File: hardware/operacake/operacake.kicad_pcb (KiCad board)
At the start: 4 copper layers, 120 x 75 mm, 129 parts, among them J1 CONN_02X20, J2 CONN_02X20, P1 ADDRESS, P20 GPIO, P22 I2S, P28 SD, P9 BASEBAND, U1 MASWSS0129, U10 74LVC1G58, U11 74LVC1G58, U12 74LVC1G58, U13 74LVC1G58, U14 74AHC1G02, U15 74AHC1G02, U16 74LVC1G19, U2 SKY13322, U3 SKY13322, U4 PCA9557, U5 TC7MBL3245CFT, U6 74LVC1G58, U7 74LVC1G58, U8 74AHC1G08, U9 74AHC1G08

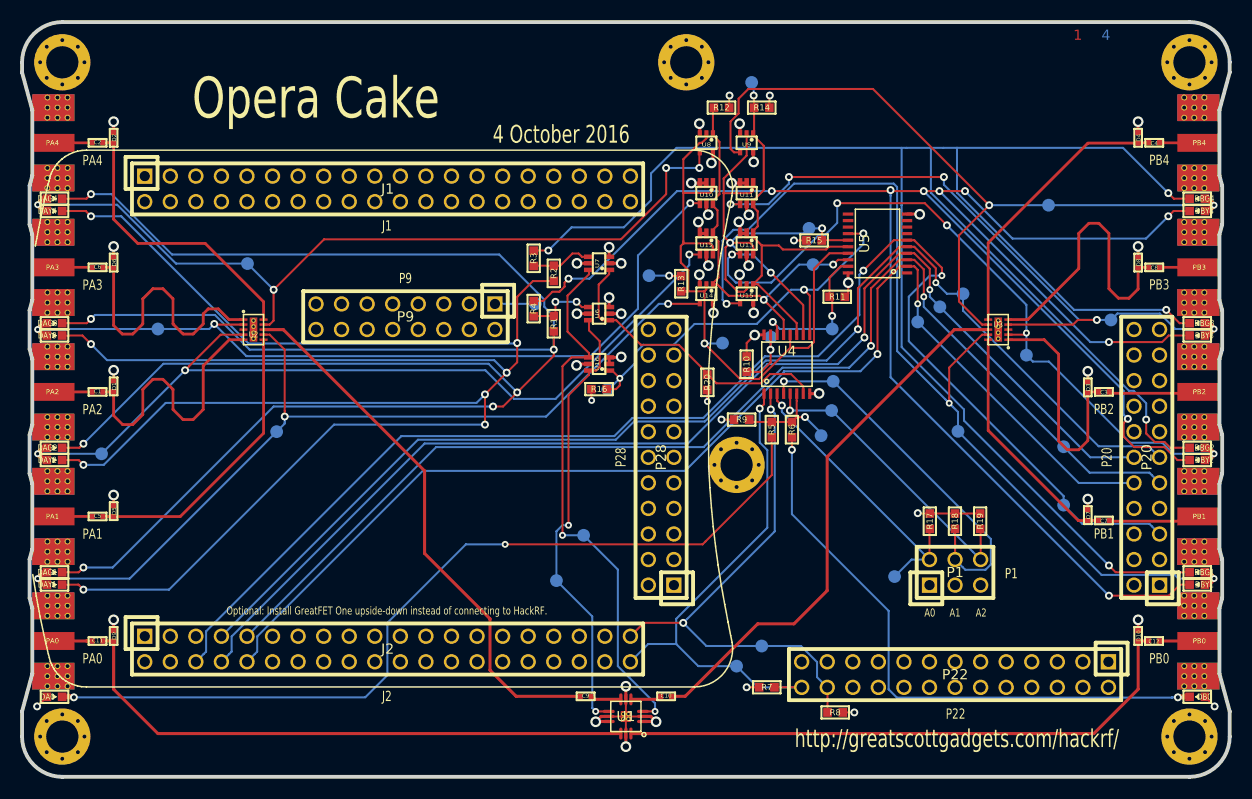
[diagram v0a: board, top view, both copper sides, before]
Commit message: Added decoupling capacitors.
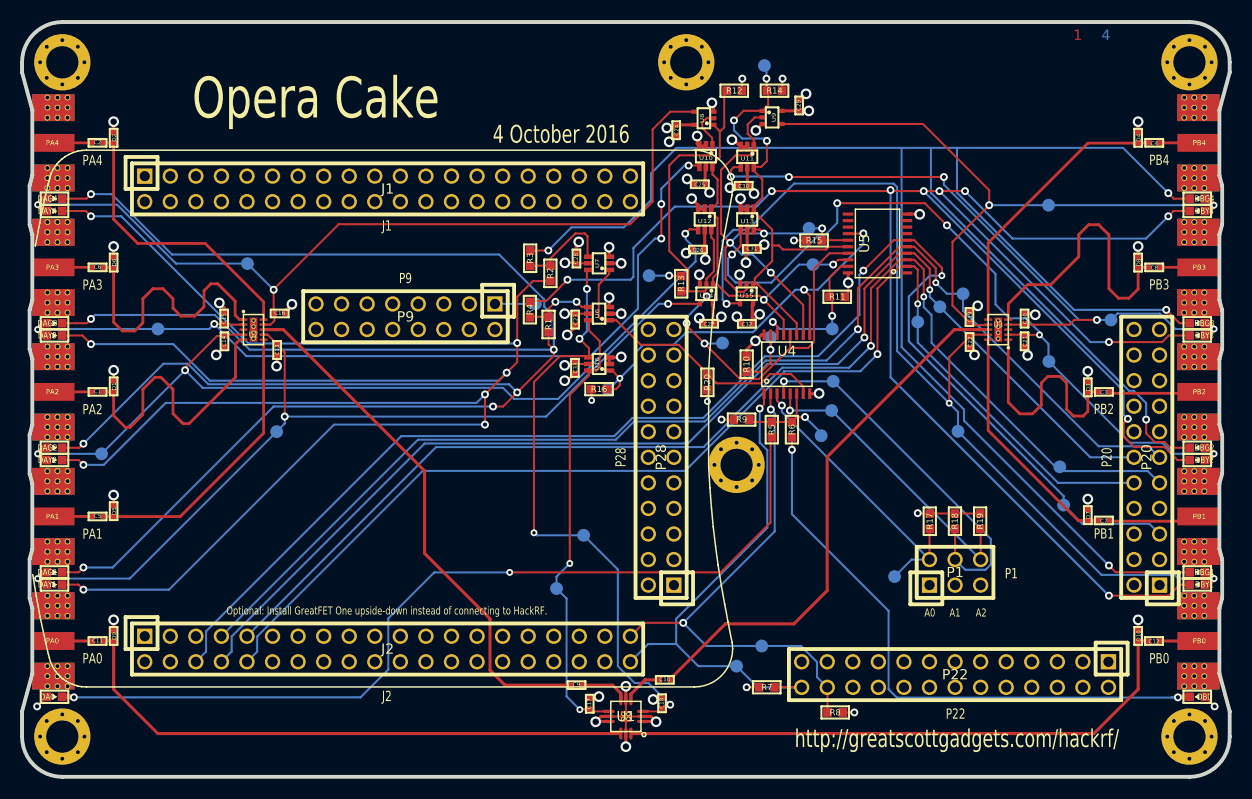
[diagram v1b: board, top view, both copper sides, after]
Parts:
- added C13: 33pF, gsg-modules:0402, F.Cu at (85.3, 132.6)
- added C14: 33pF, gsg-modules:0402, F.Cu at (80.1, 131.7)
- added C15: 33pF, gsg-modules:0402, F.Cu at (80.1, 129.5)
- added C16: 33pF, gsg-modules:0402, F.Cu at (85.6, 129.0)
- added C17: 33pF, gsg-modules:0402, F.Cu at (116.4, 167.7)
- added C18: 33pF, gsg-modules:0402, F.Cu at (123.6, 167.7)
- added C19: 33pF, gsg-modules:0402, F.Cu at (154.1, 129.3)
- added C20: 33pF, gsg-modules:0402, F.Cu at (159.6, 129.5)
- added C21: 33pF, gsg-modules:0402, F.Cu at (159.6, 131.7)
- added C22: 33pF, gsg-modules:0402, F.Cu at (154.2, 131.8)
- added C23: 100nF, gsg-modules:0402, F.Cu at (115.0, 129.6)
- added C24: 100nF, gsg-modules:0402, F.Cu at (125.0, 110.7)
- added C25: 100nF, gsg-modules:0402, F.Cu at (127.3, 116.1)
- added C26: 100nF, gsg-modules:0402, F.Cu at (127.2, 122.6)
- added C27: 100nF, gsg-modules:0402, F.Cu at (128.3, 130.0)
- added C28: 100nF, gsg-modules:0402, F.Cu at (115.1, 123.5)
- added C29: 100nF, gsg-modules:0402, F.Cu at (137.2, 108.3)
- added C30: 100nF, gsg-modules:0402, F.Cu at (131.7, 116.3)
- added C31: 100nF, gsg-modules:0402, F.Cu at (132.5, 122.5)
- added C32: 100nF, gsg-modules:0402, F.Cu at (132.0, 130.0)
- added C33: 100nF, gsg-modules:0402, F.Cu at (114.9, 134.4)
- C1, C10, C11, C12, C2, C3, C4, C5, C6, C7, C8, C9: value C -> 100nF
- moved U10 3.68 mm to (128.0, 113.3)
- moved U11 3.61 mm to (132.1, 113.4)
- moved U9 3.57 mm to (134.5, 109.5), turned to 270 degrees
- moved U8 2.45 mm to (127.8, 109.6), turned to 90 degrees
- moved U12 2.40 mm to (127.8, 119.6)
- moved U13 2.38 mm to (132.1, 119.6)
- moved TP23 2.32 mm to (162.0, 133.7)
- moved R12 2.10 mm to (130.8, 106.8)
- moved R14 2.10 mm to (134.8, 106.8)
- moved TP13 2.10 mm to (133.8, 104.3)
- moved TP2 2.04 mm to (163.1, 144.2)
- moved C10 1.64 mm to (123.9, 165.4)
- moved C9 1.44 mm to (115.1, 165.9)
- moved TP17 0.79 mm to (113.1, 156.3)
- moved R1 0.52 mm to (112.3, 130.0)
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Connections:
- J1 pad 10: (no net) -> Net-(J1-Pad10)
- J1 pad 11: (no net) -> Net-(J1-Pad11)
- J1 pad 12: (no net) -> Net-(J1-Pad12)
- J1 pad 13: (no net) -> Net-(J1-Pad13)
- J1 pad 14: (no net) -> Net-(J1-Pad14)
- J1 pad 15: (no net) -> Net-(J1-Pad15)
- J1 pad 16: (no net) -> Net-(J1-Pad16)
- J1 pad 17: (no net) -> Net-(J1-Pad17)
- J1 pad 18: (no net) -> Net-(J1-Pad18)
- J1 pad 19: (no net) -> Net-(J1-Pad19)
- J1 pad 20: (no net) -> Net-(J1-Pad20)
- J1 pad 21: (no net) -> Net-(J1-Pad21)
- J1 pad 22: (no net) -> Net-(J1-Pad22)
- J1 pad 23: (no net) -> Net-(J1-Pad23)
- J1 pad 24: (no net) -> Net-(J1-Pad24)
- J1 pad 25: (no net) -> Net-(J1-Pad25)
- J1 pad 26: (no net) -> Net-(J1-Pad26)
- J1 pad 27: (no net) -> Net-(J1-Pad27)
- J1 pad 28: (no net) -> Net-(J1-Pad28)
- J1 pad 29: (no net) -> Net-(J1-Pad29)
- J1 pad 3: (no net) -> Net-(J1-Pad3)
- J1 pad 30: (no net) -> Net-(J1-Pad30)
- J1 pad 31: (no net) -> Net-(J1-Pad31)
- J1 pad 32: (no net) -> Net-(J1-Pad32)
- J1 pad 33: (no net) -> Net-(J1-Pad33)
- J1 pad 34: (no net) -> Net-(J1-Pad34)
- J1 pad 35: (no net) -> Net-(J1-Pad35)
- J1 pad 36: (no net) -> Net-(J1-Pad36)
- J1 pad 37: (no net) -> Net-(J1-Pad37)
- J1 pad 38: (no net) -> Net-(J1-Pad38)
- J1 pad 39: (no net) -> Net-(J1-Pad39)
- J1 pad 4: (no net) -> Net-(J1-Pad4)
- J1 pad 40: (no net) -> Net-(J1-Pad40)
- J1 pad 5: (no net) -> Net-(J1-Pad5)
- J1 pad 6: (no net) -> Net-(J1-Pad6)
- J1 pad 7: (no net) -> Net-(J1-Pad7)
- J1 pad 8: (no net) -> Net-(J1-Pad8)
- J1 pad 9: (no net) -> Net-(J1-Pad9)
- J2 pad 11: (no net) -> Net-(J2-Pad11)
- J2 pad 12: (no net) -> Net-(J2-Pad12)
- J2 pad 13: (no net) -> Net-(J2-Pad13)
- J2 pad 14: (no net) -> Net-(J2-Pad14)
- J2 pad 15: (no net) -> Net-(J2-Pad15)
- J2 pad 16: (no net) -> Net-(J2-Pad16)
- J2 pad 17: (no net) -> Net-(J2-Pad17)
- J2 pad 18: (no net) -> Net-(J2-Pad18)
- J2 pad 19: (no net) -> Net-(J2-Pad19)
- J2 pad 2: (no net) -> Net-(J2-Pad2)
- J2 pad 20: (no net) -> Net-(J2-Pad20)
- J2 pad 21: (no net) -> Net-(J2-Pad21)
- J2 pad 22: (no net) -> Net-(J2-Pad22)
- J2 pad 23: (no net) -> Net-(J2-Pad23)
- J2 pad 24: (no net) -> Net-(J2-Pad24)
- J2 pad 25: (no net) -> Net-(J2-Pad25)
- J2 pad 26: (no net) -> Net-(J2-Pad26)
- J2 pad 27: (no net) -> Net-(J2-Pad27)
- J2 pad 28: (no net) -> Net-(J2-Pad28)
- J2 pad 29: (no net) -> Net-(J2-Pad29)
- J2 pad 3: (no net) -> Net-(J2-Pad3)
- J2 pad 30: (no net) -> Net-(J2-Pad30)
- J2 pad 31: (no net) -> Net-(J2-Pad31)
- J2 pad 32: (no net) -> Net-(J2-Pad32)
- J2 pad 33: (no net) -> Net-(J2-Pad33)
- J2 pad 34: (no net) -> Net-(J2-Pad34)
- J2 pad 35: (no net) -> Net-(J2-Pad35)
- J2 pad 36: (no net) -> Net-(J2-Pad36)
- J2 pad 37: (no net) -> Net-(J2-Pad37)
- J2 pad 38: (no net) -> Net-(J2-Pad38)
- J2 pad 4: (no net) -> Net-(J2-Pad4)
- J2 pad 5: (no net) -> Net-(J2-Pad5)
- P20 pad 1: (no net) -> Net-(P20-Pad1)
- P20 pad 14: (no net) -> Net-(P20-Pad14)
- P20 pad 16: (no net) -> Net-(P20-Pad16)
- P20 pad 17: (no net) -> Net-(P20-Pad17)
- P20 pad 18: (no net) -> Net-(P20-Pad18)
- P20 pad 2: (no net) -> Net-(P20-Pad2)
- P20 pad 20: (no net) -> Net-(P20-Pad20)
- P20 pad 21: (no net) -> Net-(P20-Pad21)
- P20 pad 22: (no net) -> Net-(P20-Pad22)
- P20 pad 4: (no net) -> Net-(P20-Pad4)
- P20 pad 6: (no net) -> Net-(P20-Pad6)
- P20 pad 7: (no net) -> Net-(P20-Pad7)
- P20 pad 8: (no net) -> Net-(P20-Pad8)
- P22 pad 1: (no net) -> Net-(P22-Pad1)
- P22 pad 12: (no net) -> Net-(P22-Pad12)
- P22 pad 13: (no net) -> Net-(P22-Pad13)
- P22 pad 14: (no net) -> Net-(P22-Pad14)
- P22 pad 15: (no net) -> Net-(P22-Pad15)
- P22 pad 16: (no net) -> Net-(P22-Pad16)
- P22 pad 17: (no net) -> Net-(P22-Pad17)
- P22 pad 19: (no net) -> Net-(P22-Pad19)
- P22 pad 2: (no net) -> Net-(P22-Pad2)
- P22 pad 20: (no net) -> Net-(P22-Pad20)
- P22 pad 21: (no net) -> Net-(P22-Pad21)
- P22 pad 22: (no net) -> Net-(P22-Pad22)
- P22 pad 23: (no net) -> Net-(P22-Pad23)
- P22 pad 25: (no net) -> Net-(P22-Pad25)
- P22 pad 3: (no net) -> Net-(P22-Pad3)
- P22 pad 5: (no net) -> Net-(P22-Pad5)
- P22 pad 6: (no net) -> Net-(P22-Pad6)
- P22 pad 7: (no net) -> Net-(P22-Pad7)
- P22 pad 8: (no net) -> Net-(P22-Pad8)
- P22 pad 9: (no net) -> Net-(P22-Pad9)
- P28 pad 10: (no net) -> Net-(P28-Pad10)
- P28 pad 11: (no net) -> Net-(P28-Pad11)
- P28 pad 13: (no net) -> Net-(P28-Pad13)
- P28 pad 14: (no net) -> Net-(P28-Pad14)
- P28 pad 15: (no net) -> Net-(P28-Pad15)
- P28 pad 16: (no net) -> Net-(P28-Pad16)
- P28 pad 17: (no net) -> Net-(P28-Pad17)
- P28 pad 18: (no net) -> Net-(P28-Pad18)
- P28 pad 19: (no net) -> Net-(P28-Pad19)
- P28 pad 20: (no net) -> Net-(P28-Pad20)
- P28 pad 21: (no net) -> Net-(P28-Pad21)
- P28 pad 22: (no net) -> Net-(P28-Pad22)
- P28 pad 3: (no net) -> Net-(P28-Pad3)
- P28 pad 4: (no net) -> Net-(P28-Pad4)
- P28 pad 5: (no net) -> Net-(P28-Pad5)
- P28 pad 6: (no net) -> Net-(P28-Pad6)
- P28 pad 7: (no net) -> Net-(P28-Pad7)
- P28 pad 8: (no net) -> Net-(P28-Pad8)
- P28 pad 9: (no net) -> Net-(P28-Pad9)
- P9 pad 10: (no net) -> Net-(P9-Pad10)
- P9 pad 11: (no net) -> Net-(P9-Pad11)
- P9 pad 12: (no net) -> Net-(P9-Pad12)
- P9 pad 13: (no net) -> Net-(P9-Pad13)
- P9 pad 4: (no net) -> Net-(P9-Pad4)
- P9 pad 5: (no net) -> Net-(P9-Pad5)
- P9 pad 6: (no net) -> Net-(P9-Pad6)
- P9 pad 7: (no net) -> Net-(P9-Pad7)
- U2 pad 3: (no net) -> Net-(U2-Pad3)
- U3 pad 3: (no net) -> Net-(U3-Pad3)
- U5 pad 1: (no net) -> Net-(U5-Pad1)
- U5 pad 11: (no net) -> Net-(U5-Pad11)
- U5 pad 12: (no net) -> Net-(U5-Pad12)
- U5 pad 13: (no net) -> Net-(U5-Pad13)
- U5 pad 7: (no net) -> Net-(U5-Pad7)
- U5 pad 8: (no net) -> Net-(U5-Pad8)
- U5 pad 9: (no net) -> Net-(U5-Pad9)
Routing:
- net GND: track 55.6 -> 85.6 mm, vias 29 -> 49
- net VCC: track 34.9 -> 53.0 mm
- net /U3V3: track 75.8 -> 65.4 mm
- net /U3CTRL1: track 38.1 -> 45.4 mm, vias 1 -> 3
- net /U1VC1: track 54.0 -> 60.1 mm, vias 2 -> 4
- net /U2CTRL0: track 62.2 -> 68.1 mm, vias 1 -> 3
- net /U2V2: track 82.1 -> 86.6 mm, vias 3 -> 5
- net Net-(R2-Pad2): track 6.15 -> 10.1 mm
- net /U2V1: track 86.6 -> 90.0 mm
- net /U3V2: track 73.5 -> 76.8 mm
- net /U2V4: track 84.1 -> 87.3 mm, vias 4 -> 2
- net /U2CTRL1: track 39.0 -> 41.9 mm
- net Net-(DA0-Pad1): track 86.5 -> 89.1 mm
- net Net-(C9-Pad1): track 3.09 -> 5.14 mm
- net /EXT_U2CTRL0: track 120.9 -> 122.6 mm
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
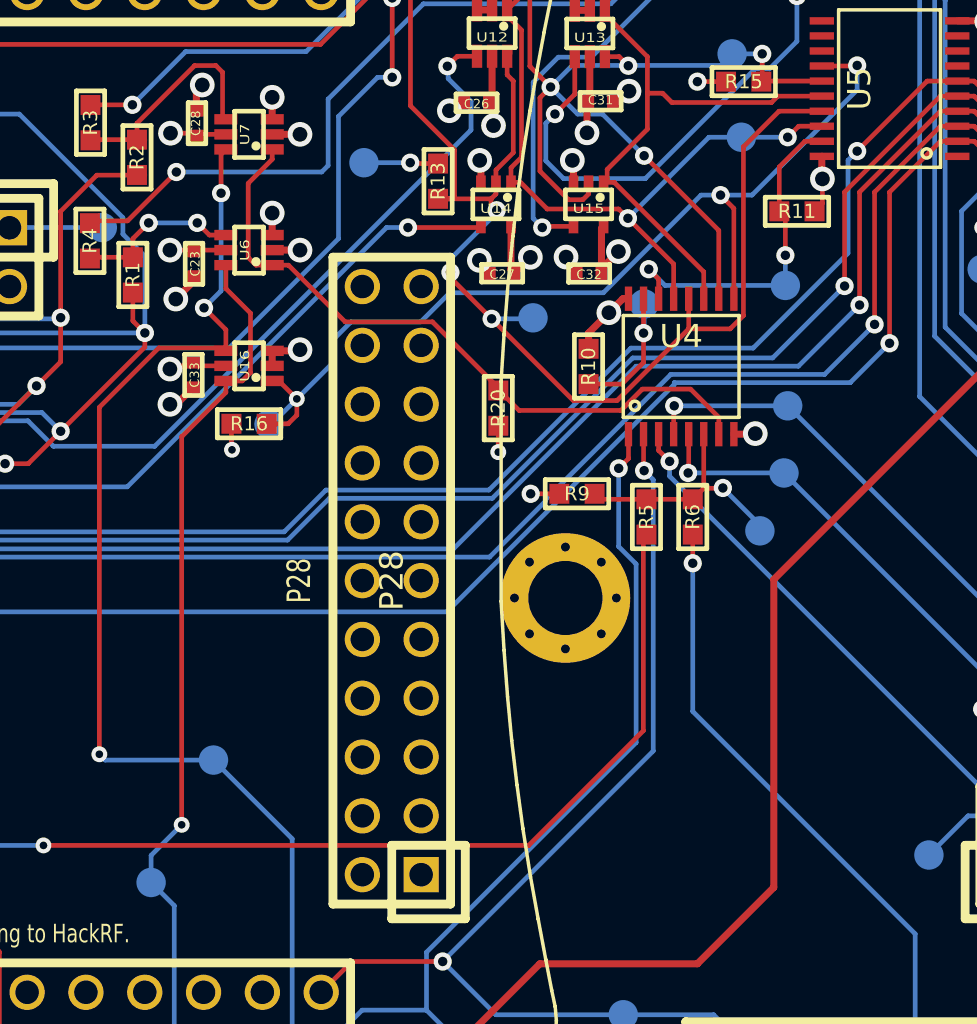
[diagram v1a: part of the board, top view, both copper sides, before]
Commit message: more decoupling caps and remove one GND from P22
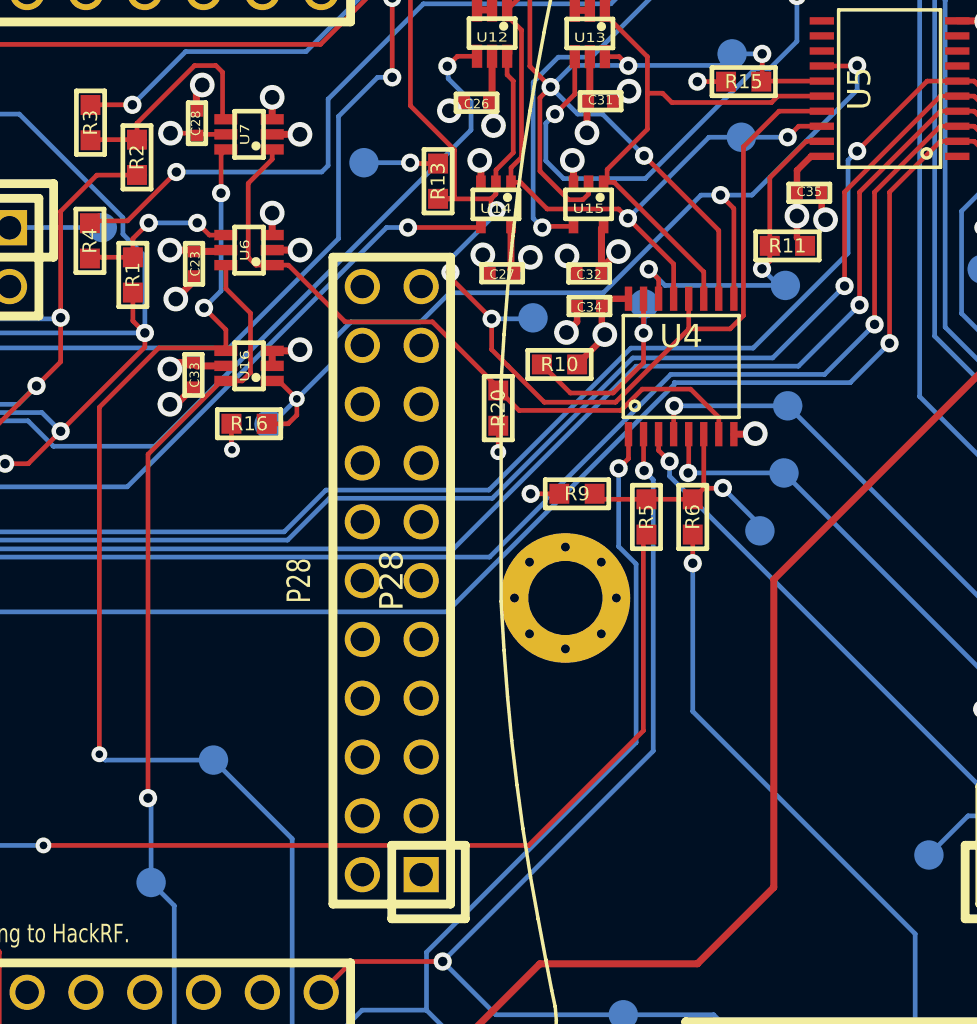
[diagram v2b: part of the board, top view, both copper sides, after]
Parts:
- added C34: 100nF, gsg-modules:0402, F.Cu at (132.0, 131.4)
- added C35: 100nF, gsg-modules:0402, F.Cu at (141.5, 126.5)
- moved R11 1.55 mm to (140.6, 128.8)
- moved R10 1.26 mm to (130.7, 133.9), turned to 0 degrees
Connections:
- P20 pad 13: GND -> Net-(P20-Pad13)
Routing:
- net VCC: track 53.0 -> 56.8 mm
- net GND: track 85.6 -> 89.1 mm, vias 49 -> 52
- net /!RESET: track 6.78 -> 9.48 mm
- net /!OE: track 15.2 -> 16.2 mm
- net /U2CTRL0: track 68.1 -> 69.0 mm
- net (no net): vias 1 -> 0
